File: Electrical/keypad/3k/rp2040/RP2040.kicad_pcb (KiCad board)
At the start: 4 copper layers, 64.2 x 66.2 mm, 97 parts, among them J1 Conn_01x02_Socket, J2 Conn_01x04_Socket, P1 USB-TYPE-C-016, Q1 BSS138, Q2 BSS138, SW1 KAN0644-0551B1-A, SW2 KAN0644-0551B1-A, SW3 KAN0644-0551B1-A, SW4 TS-1187A-B-A-B, SW5 TS-1187A-B-A-B, U1 ME6212C33M5G, U2 W25Q16JVSS, U3 PRTR5V0U2X, U4 RP2040, U5 SLSS49E, U6 SLSS49E, U7 SLSS49E, Y1 12MHz

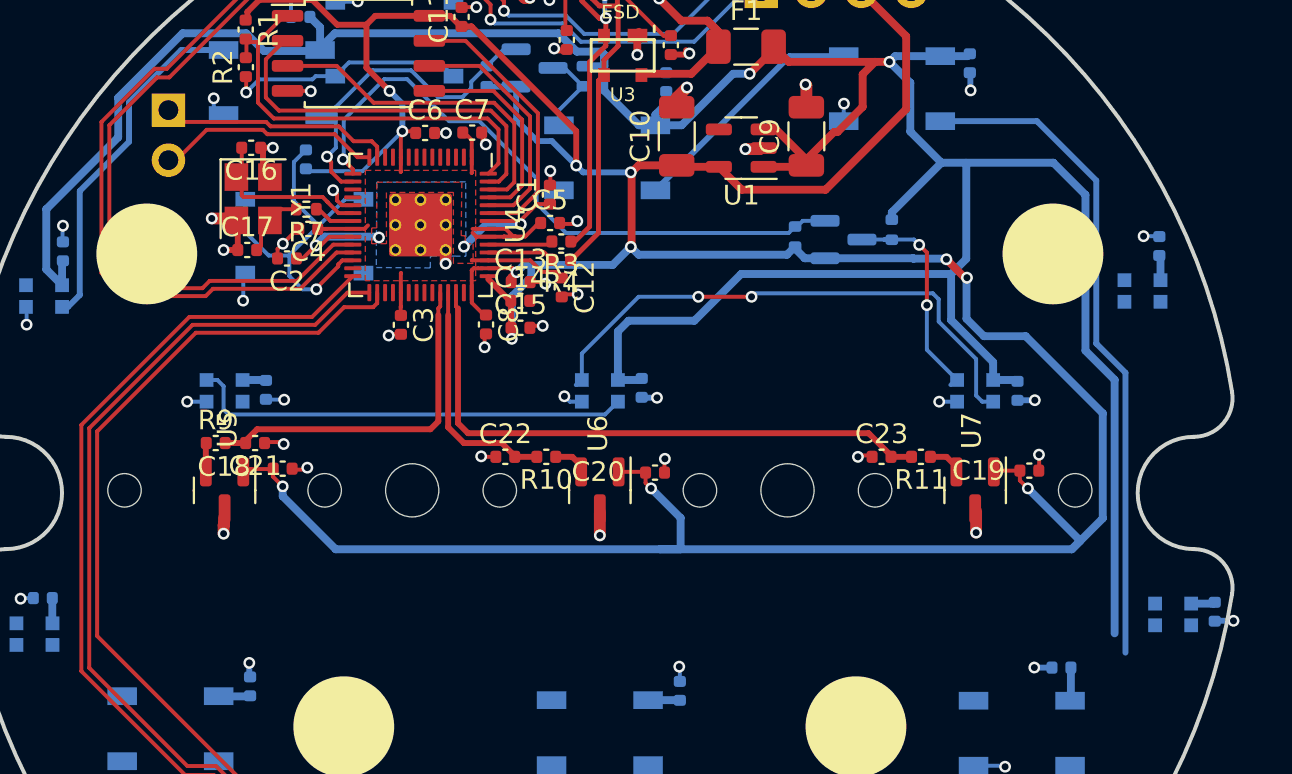
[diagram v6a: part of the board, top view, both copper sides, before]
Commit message: dodge the screw holes so that the signals never have a chance of touching the metal screws
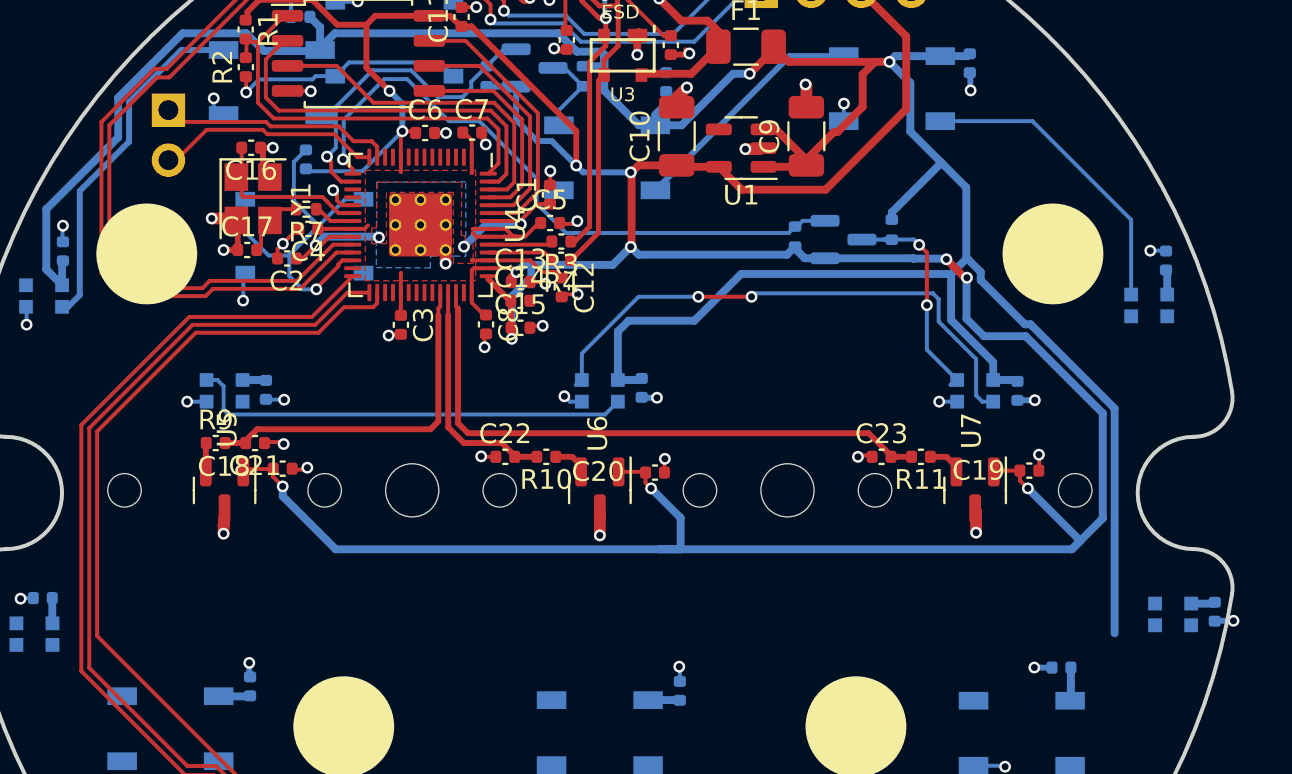
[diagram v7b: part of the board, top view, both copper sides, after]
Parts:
- REF**: moved to B.Cu
- moved C26 0.81 mm to (128.7, 88.3)
- moved D3 0.81 mm to (127.9, 90.6)
- moved REF** 0.10 mm to (77.0, 88.0)
- turned REF** to 180 degrees
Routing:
- net Net-(D2-DOUT): track 33.7 -> 15.6 mm
- net +5V: track 170.3 -> 162.3 mm

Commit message: finishes PCB layout
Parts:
- moved C28 3.20 mm to (125.5, 111.4), turned to -90 degrees
- moved C27 2.11 mm to (129.4, 105.0), turned to 180 degrees
- moved SW4 2.08 mm to (90.7, 78.9)
- moved C29 1.26 mm to (82.5, 111.2), turned to -90 degrees
- moved C31 0.97 mm to (95.0, 124.7), turned to -90 degrees
- moved C25 0.84 mm to (118.7, 79.2)
- moved D2 0.84 mm to (114.8, 80.5)
- moved D11 0.80 mm to (72.5, 90.5)
- moved C32 0.77 mm to (113.0, 123.9)
- moved D6 0.73 mm to (109.0, 126.0)
- moved D4 0.71 mm to (129.0, 107.0)
- moved C30 0.62 mm to (104.0, 110.8), turned to -90 degrees
- moved C33 0.60 mm to (72.2, 105.2), turned to 0 degrees
- moved D9 0.50 mm to (78.5, 112.5)
- moved D10 0.42 mm to (71.0, 107.0)
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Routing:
- net +5V: track 162.3 -> 300.1 mm
- net Net-(D7-DOUT): track 0.00 -> 28.9 mm
- net Net-(D8-DOUT): track 0.00 -> 28.3 mm
- net Net-(D5-DOUT): track 0.00 -> 27.6 mm
- net Net-(D6-DOUT): track 0.00 -> 25.2 mm
- net Net-(D10-DO): track 0.00 -> 21.0 mm
- net Net-(D3-DO): track 0.00 -> 16.7 mm
- net Net-(D10-DI): track 0.00 -> 15.1 mm
- net Net-(D4-DO): track 0.00 -> 14.8 mm
- net GND: track 64.5 -> 72.3 mm, vias 60 -> 226
- net Net-(R2-Pad1): track 12.3 -> 16.4 mm, vias 1 -> 3
- net +3V3: track 200.8 -> 204.2 mm
- net SWDIO: track 64.9 -> 65.7 mm
- net Net-(D2-DOUT): track 15.6 -> 15.0 mm
- net SWCLK: track 60.2 -> 60.7 mm
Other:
- board text added: "3V3"
- board text added: "GND"
- board text added: "SCL"
- board text added: "SDA"
- board text added: "SWC"
- board text added: "SWD"
- board text removed: "SW3"
